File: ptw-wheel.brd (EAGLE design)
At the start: 54 x 45 mm, 5 parts

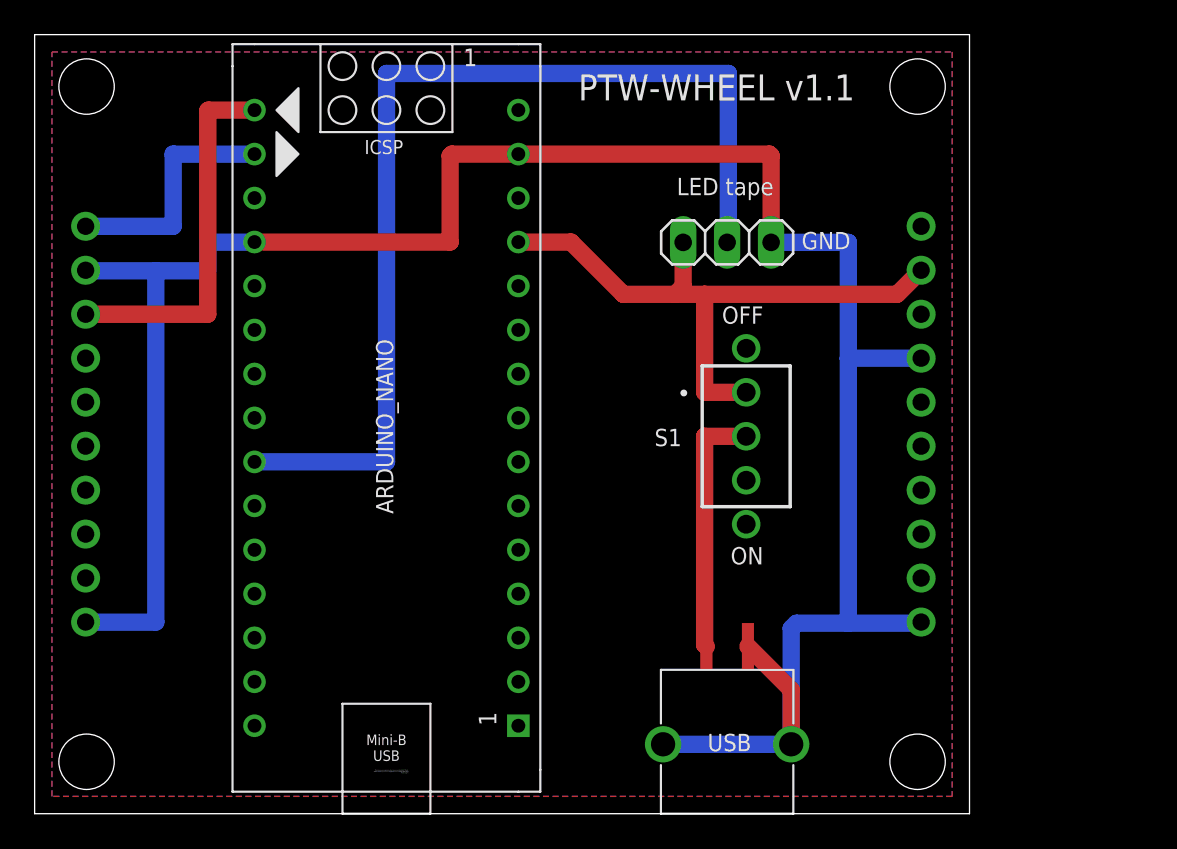
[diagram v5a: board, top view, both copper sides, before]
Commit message: - Replace toggle switch - Adjust positions
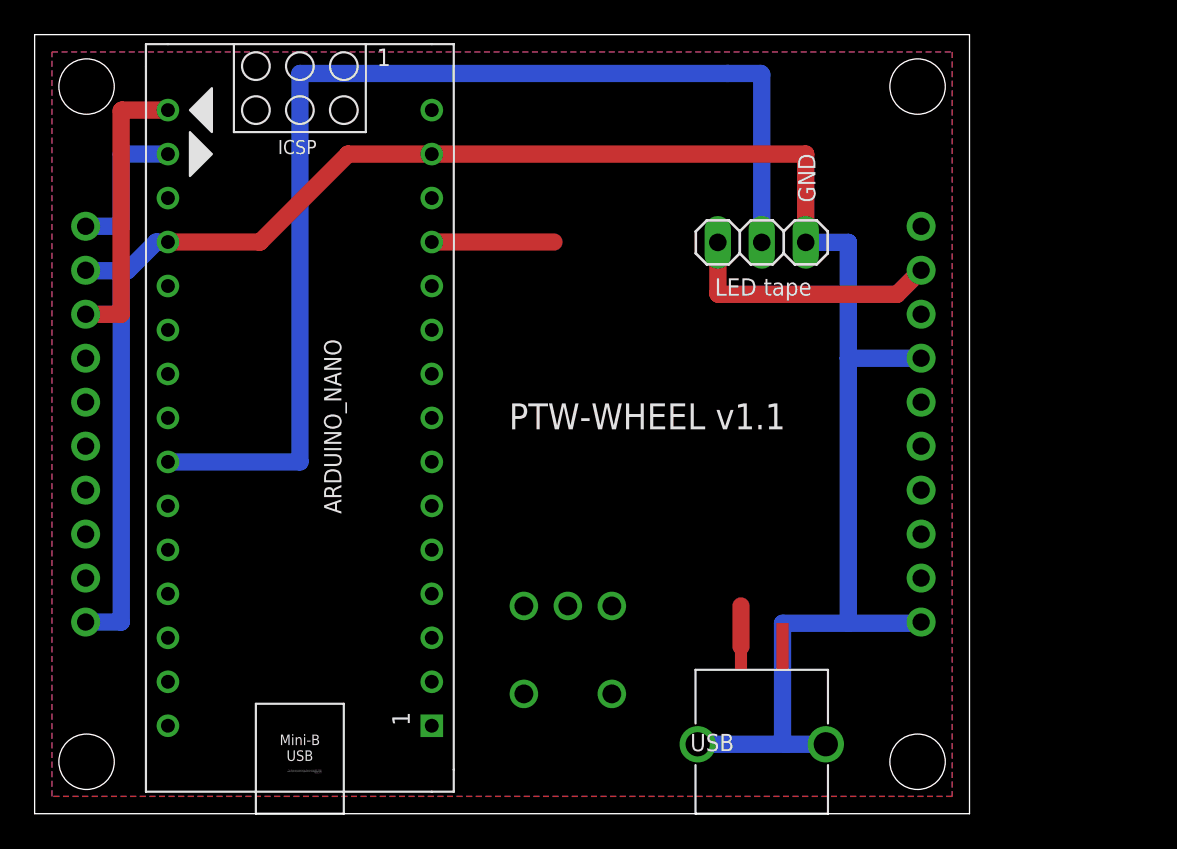
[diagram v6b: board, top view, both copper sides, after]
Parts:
- removed S1: 2MS1-T1-B4-M2-Q-E, 2MS1-T1-B4-VS2-Q-E:2MS1-T1-B4-M2-Q-E
- added U$1: MTS-12PB-5P, toggle-switch:MTS-12PB-5P
- moved ARDUINO_NANO 5.00 mm to (15.3, 25.4)
- moved JP1 2.00 mm to (42.0, 33.0)
- moved USB 2.00 mm to (42.0, 8.31)
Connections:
- net +5V: now also U$1.3; no longer S1.1
- net N$1: now also U$1.2; no longer S1.2
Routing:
- net +5V: track 36.3 -> 22.4 mm
- net N$1: track 14.6 -> 2.34 mm
- net GND: track 134.8 -> 123.0 mm
- net N$3: track 59.6 -> 66.5 mm
- net N$5: track 21.5 -> 16.5 mm
- net N$4: track 13.9 -> 8.92 mm
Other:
- board text removed: "OFF"
- board text removed: "ON"

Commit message: Adjust position of USBcon and LED tapes to avoid confliction with foots
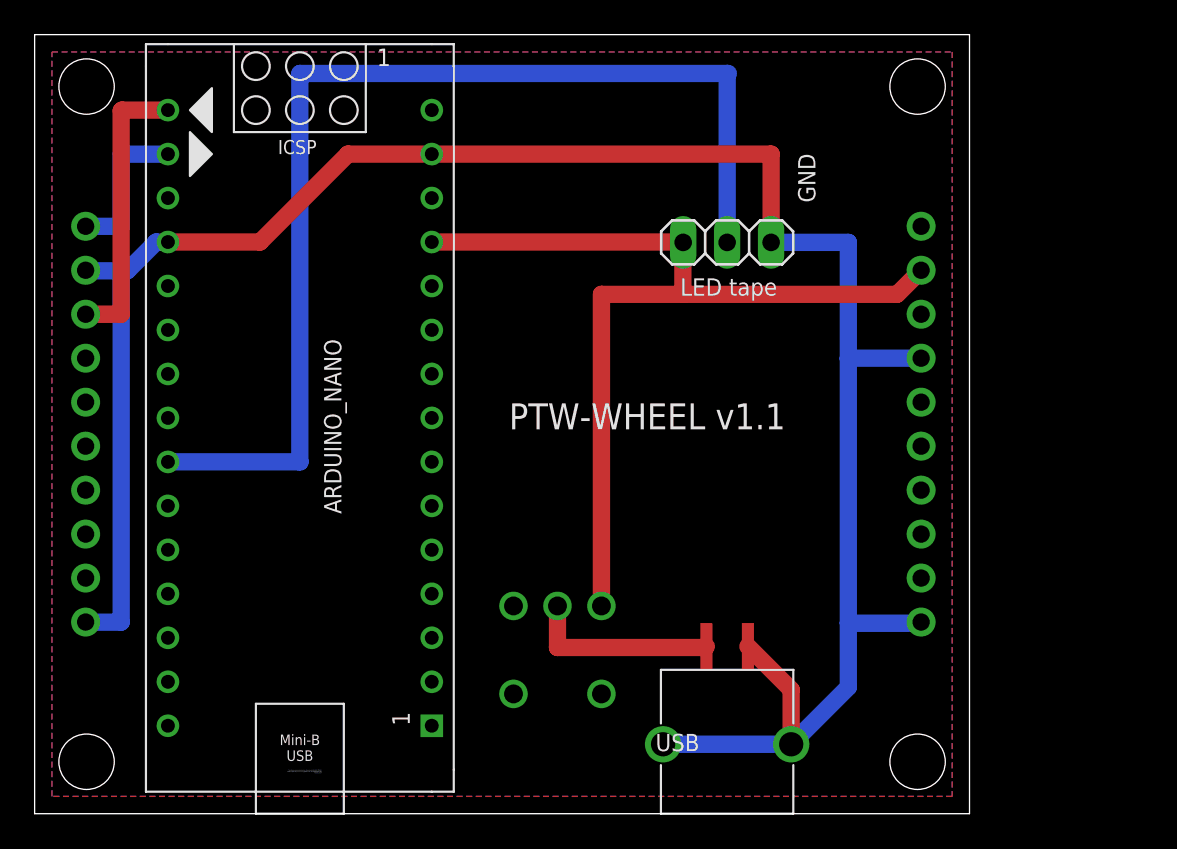
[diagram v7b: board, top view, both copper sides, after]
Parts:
- moved JP1 2.00 mm to (40.0, 33.0)
- moved USB 2.00 mm to (40.0, 8.31)
- moved U$1 0.60 mm to (30.2, 12.0)
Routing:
- net +5V: track 22.4 -> 54.6 mm
- net N$1: track 2.34 -> 11.0 mm
- net GND: track 123.0 -> 127.2 mm
- net N$3: track 66.5 -> 64.6 mm
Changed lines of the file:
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@@
 <layers>
 <layer number="1" name="Top" color="4" fill="1" visible="yes" active="yes"/>
-<layer number="16" name="Bottom" color="1" fill="1" visible="yes" active="yes"/>
+<layer number="16" name="Bottom" color="1" fill="1" visible="no" active="yes"/>
 <layer number="17" name="Pads" color="2" fill="1" visible="yes" active="yes"/>
 <layer number="18" name="Vias" color="2" fill="1" visible="yes" active="yes"/>
@@
 <attribute name="VALUE" x="19.86" y="7.62" size="1.27" layer="21" font="vector" rot="R90"/>
 </element>
-<element name="JP1" library="pinhead" library_urn="urn:adsk.eagle:library:325" package="1X03" package3d_urn="urn:adsk.eagle:package:22458/2" value="LED tape" x="42" y="33" smashed="yes">
-<attribute name="VALUE" x="39.29" y="29.925" size="1" layer="25"/>
+<element name="JP1" library="pinhead" library_urn="urn:adsk.eagle:library:325" package="1X03" package3d_urn="urn:adsk.eagle:package:22458/2" value="LED tape" x="40" y="33" smashed="yes">
+<attribute name="VALUE" x="37.29" y="29.925" size="1" layer="25"/>
 </element>
 <element name="KONASHI" library="konashiv2" package="KONASHI" value="KONASHI2.0" x="1" y="6" smashed="yes"/>
-<element name="USB" library="usbcon" package="USBCON" value="USBCON" x="42" y="8.31" smashed="yes" rot="R180">
-<attribute name="NAME" x="40.4" y="4.61" size="1" layer="25" rot="R180"/>
+<element name="USB" library="usbcon" package="USBCON" value="USBCON" x="40" y="8.31" smashed="yes" rot="R180">
+<attribute name="NAME" x="38.4" y="4.61" size="1" layer="25" rot="R180"/>
 </element>
-<element name="U$1" library="toggle-switch" package="MTS-12PB-5P" value="MTS-12PB-5P" x="30.8" y="12" smashed="yes" rot="MR90">
-<attribute name="VALUE" x="36.218" y="6.531" size="1.27" layer="28" rot="MR90" align="center"/>
+<element name="U$1" library="toggle-switch" package="MTS-12PB-5P" value="MTS-12PB-5P" x="30.2" y="12" smashed="yes" rot="MR90">
+<attribute name="VALUE" x="35.618" y="6.531" size="1.27" layer="28" rot="MR90" align="center"/>
 </element>
 </elements>
@@
 <wire x1="15.32668125" y1="42.75648125" x2="40" y2="42.75648125" width="1" layer="16"/>
 <wire x1="40" y1="42.75648125" x2="40.071040625" y2="42.75648125" width="1" layer="16"/>
-<wire x1="42" y1="33" x2="42" y2="42.7" width="1" layer="16"/>
-<wire x1="42" y1="42.7" x2="41.94351875" y2="42.75648125" width="1" layer="16"/>
-<wire x1="41.94351875" y1="42.75648125" x2="40.071040625" y2="42.75648125" width="1" layer="16"/>
+<wire x1="40" y1="33" x2="40" y2="42.75648125" width="1" layer="16"/>
 </signal>
 <signal name="N$4">
@@
 <contactref element="ARDUINO_NANO" pad="12"/>
 <wire x1="51.205640625" y1="31.389840625" x2="49.8158" y2="30" width="1" layer="1"/>
-<wire x1="49.8158" y1="30" x2="39.5" y2="30" width="1" layer="1"/>
 <contactref element="U$1" pad="3"/>
-<wire x1="39.46" y1="33" x2="39.46" y2="30.04" width="1" layer="1"/>
-<wire x1="39.5" y1="30" x2="39.46" y2="30.04" width="1" layer="1"/>
-<wire x1="30" y1="33.02" x2="22.94" y2="33.02" width="1" layer="1"/>
-<wire x1="30" y1="33.02" x2="39.46" y2="33" width="0" layer="19" extent="1-1"/>
-<wire x1="33.34" y1="12" x2="39.5" y2="30" width="0" layer="19" extent="1-1"/>
+<wire x1="22.94" y1="33.02" x2="37.44" y2="33.02" width="1" layer="1"/>
+<wire x1="37.44" y1="33.02" x2="37.46" y2="33" width="1" layer="1"/>
+<wire x1="49.8158" y1="30" x2="37.5" y2="30" width="1" layer="1"/>
+<wire x1="37.5" y1="30" x2="37.44" y2="30.06" width="1" layer="1"/>
+<wire x1="37.44" y1="30.06" x2="37.44" y2="33.02" width="1" layer="1"/>
+<wire x1="32.74" y1="12" x2="32.74" y2="30" width="1" layer="1"/>
+<wire x1="32.74" y1="30" x2="37.5" y2="30" width="1" layer="1"/>
 </signal>
 <signal name="GND">
@@
 <wire x1="13.02" y1="33.02" x2="18.1" y2="38.1" width="1" layer="1"/>
 <wire x1="18.1" y1="38.1" x2="22.94" y2="38.1" width="1" layer="1"/>
-<wire x1="38.3" y1="4.01" x2="43.4" y2="4.01" width="1" layer="16"/>
+<wire x1="36.3" y1="4.01" x2="43.7" y2="4.01" width="1" layer="16"/>
 <polygon width="1" layer="1">
 <vertex x="1" y="44"/>
@@
 <vertex x="1" y="1"/>
 </polygon>
-<wire x1="43.4" y1="4.01" x2="45.7" y2="4.01" width="1" layer="16"/>
 <wire x1="5.36" y1="31.36" x2="5" y2="31.36" width="1" layer="16"/>
 <wire x1="5" y1="31.36" x2="2.97548125" y2="31.36" width="1" layer="16"/>
 <wire x1="2.97548125" y1="31.36" x2="2.945640625" y2="31.389840625" width="1" layer="16"/>
 <wire x1="2.945640625" y1="11.069840625" x2="5" y2="11.069840625" width="1" layer="16"/>
-<wire x1="44.54" y1="33" x2="47" y2="33" width="1" layer="16"/>
+<wire x1="42.54" y1="33" x2="47" y2="33" width="1" layer="16"/>
 <wire x1="47" y1="33" x2="47" y2="26.3" width="1" layer="16"/>
 <wire x1="47" y1="26.3" x2="47" y2="11" width="1" layer="16"/>
@@
 <wire x1="47.009840625" y1="26.309840625" x2="47" y2="26.3" width="1" layer="16"/>
 <wire x1="5" y1="11.069840625" x2="5" y2="31.36" width="1" layer="16"/>
-<wire x1="44.54" y1="33" x2="44.54" y2="38.1" width="1" layer="1"/>
-<wire x1="44.54" y1="38.1" x2="22.94" y2="38.1" width="1" layer="1"/>
 <wire x1="51.205640625" y1="11.069840625" x2="51.1358" y2="11" width="1" layer="16"/>
 <wire x1="51.1358" y1="11" x2="47" y2="11" width="1" layer="16"/>
-<wire x1="47" y1="11" x2="43.2" y2="11" width="1" layer="16"/>
-<wire x1="43.2" y1="4.21" x2="43.4" y2="4.01" width="1" layer="16"/>
-<wire x1="43.2" y1="11" x2="43.2" y2="4.21" width="1" layer="16"/>
-<wire x1="43.2" y1="11" x2="43.2" y2="9.66" width="0" layer="19" extent="1-16"/>
+<wire x1="43.7" y1="4.01" x2="47" y2="7.31" width="1" layer="16"/>
+<wire x1="47" y1="11" x2="47" y2="7.31" width="1" layer="16"/>
+<wire x1="42.54" y1="33" x2="42.54" y2="38.1" width="1" layer="1"/>
+<wire x1="42.54" y1="38.1" x2="22.94" y2="38.1" width="1" layer="1"/>
+<wire x1="41.2" y1="9.66" x2="43.7" y2="7.16" width="1" layer="1"/>
+<wire x1="43.7" y1="7.16" x2="43.7" y2="4.01" width="1" layer="1"/>
 </signal>
 <signal name="N$1">
 <contactref element="USB" pad="5V"/>
 <contactref element="U$1" pad="2"/>
-<wire x1="40.8" y1="12" x2="40.8" y2="9.66" width="1" layer="1"/>
-<wire x1="30.8" y1="12" x2="40.8" y2="12" width="0" layer="19" extent="1-1"/>
+<wire x1="30.2" y1="12" x2="30.2" y2="9.6" width="1" layer="1"/>
+<wire x1="30.2" y1="9.6" x2="38.74" y2="9.6" width="1" layer="1"/>
+<wire x1="38.74" y1="9.6" x2="38.8" y2="9.66" width="1" layer="1"/>
 </signal>
 </signals>

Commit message: Move switch position
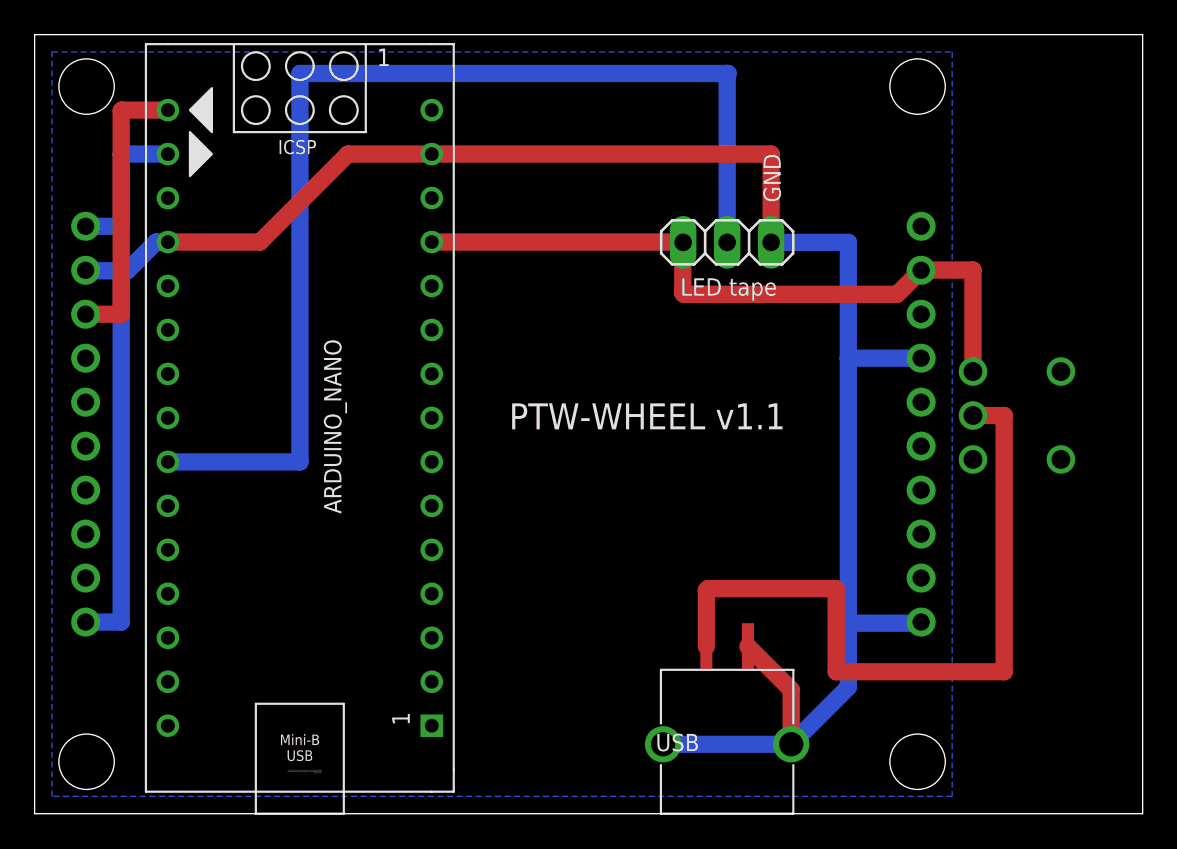
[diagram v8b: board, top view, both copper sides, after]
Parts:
- moved U$1 26.4 mm to (54.2, 23.0), turned to 0 degrees
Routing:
- net N$1: track 11.0 -> 41.9 mm
- net +5V: track 54.6 -> 40.7 mm
- removed copper zone on layer 1, net GND
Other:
- board size 54 x 45 mm -> 64 x 45 mm
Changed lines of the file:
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@@
 <board>
 <plain>
-<wire x1="0" y1="0" x2="54" y2="0" width="0" layer="20"/>
-<wire x1="54" y1="0" x2="54" y2="45" width="0" layer="20"/>
-<wire x1="54" y1="45" x2="0" y2="45" width="0" layer="20"/>
+<wire x1="0" y1="0" x2="64" y2="0" width="0" layer="20"/>
+<wire x1="64" y1="0" x2="64" y2="45" width="0" layer="20"/>
+<wire x1="64" y1="45" x2="0" y2="45" width="0" layer="20"/>
 <wire x1="0" y1="45" x2="0" y2="0" width="0" layer="20"/>
 <hole x="3" y="42" drill="3.2"/>
@@
 <hole x="51" y="42" drill="3.2"/>
 <text x="27.4" y="22.2" size="1.5" layer="25">PTW-WHEEL v1.1</text>
-<text x="45.1" y="35.3" size="1" layer="25" rot="R90">GND</text>
+<text x="43.1" y="35.3" size="1" layer="25" rot="R90">GND</text>
 </plain>
 <attributes>
@@
 <attribute name="NAME" x="38.4" y="4.61" size="1" layer="25" rot="R180"/>
 </element>
-<element name="U$1" library="toggle-switch" package="MTS-12PB-5P" value="MTS-12PB-5P" x="30.2" y="12" smashed="yes" rot="MR90">
-<attribute name="VALUE" x="35.618" y="6.531" size="1.27" layer="28" rot="MR90" align="center"/>
+<element name="U$1" library="toggle-switch" package="MTS-12PB-5P" value="MTS-12PB-5P" x="54.2" y="23" smashed="yes" rot="MR0">
+<attribute name="VALUE" x="59.669" y="28.418" size="1.27" layer="28" rot="MR0" align="center"/>
 </element>
 </elements>
@@
 <wire x1="37.5" y1="30" x2="37.44" y2="30.06" width="1" layer="1"/>
 <wire x1="37.44" y1="30.06" x2="37.44" y2="33.02" width="1" layer="1"/>
-<wire x1="32.74" y1="12" x2="32.74" y2="30" width="1" layer="1"/>
-<wire x1="32.74" y1="30" x2="37.5" y2="30" width="1" layer="1"/>
+<wire x1="54.2" y1="25.54" x2="54.2" y2="31.4" width="1" layer="1"/>
+<wire x1="54.2" y1="31.4" x2="51.2158" y2="31.4" width="1" layer="1"/>
+<wire x1="51.2158" y1="31.4" x2="51.205640625" y2="31.389840625" width="1" layer="1"/>
 </signal>
 <signal name="GND">
@@
 <wire x1="18.1" y1="38.1" x2="22.94" y2="38.1" width="1" layer="1"/>
 <wire x1="36.3" y1="4.01" x2="43.7" y2="4.01" width="1" layer="16"/>
-<polygon width="1" layer="1">
-<vertex x="1" y="44"/>
-<vertex x="53" y="44"/>
-<vertex x="53" y="1"/>
-<vertex x="1" y="1"/>
-</polygon>
 <polygon width="1" layer="16">
 <vertex x="1" y="44"/>
@@
 <contactref element="USB" pad="5V"/>
 <contactref element="U$1" pad="2"/>
-<wire x1="30.2" y1="12" x2="30.2" y2="9.6" width="1" layer="1"/>
-<wire x1="30.2" y1="9.6" x2="38.74" y2="9.6" width="1" layer="1"/>
-<wire x1="38.74" y1="9.6" x2="38.8" y2="9.66" width="1" layer="1"/>
+<wire x1="54.2" y1="23" x2="56" y2="23" width="1" layer="1"/>
+<wire x1="56" y1="23" x2="56" y2="8.2" width="1" layer="1"/>
+<wire x1="56" y1="8.2" x2="46.3" y2="8.2" width="1" layer="1"/>
+<wire x1="46.3" y1="8.2" x2="46.3" y2="13" width="1" layer="1"/>
+<wire x1="46.3" y1="13" x2="38.9" y2="13" width="1" layer="1"/>
+<wire x1="38.9" y1="13" x2="38.8" y2="12.9" width="1" layer="1"/>
+<wire x1="38.8" y1="12.9" x2="38.8" y2="9.66" width="1" layer="1"/>
 </signal>
 </signals>
